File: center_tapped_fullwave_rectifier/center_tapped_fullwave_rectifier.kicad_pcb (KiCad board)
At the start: 2 copper layers, 47.5 x 21 mm, 5 parts, among them J1 Screw_Terminal_01x03, J2 Screw_Terminal_01x02

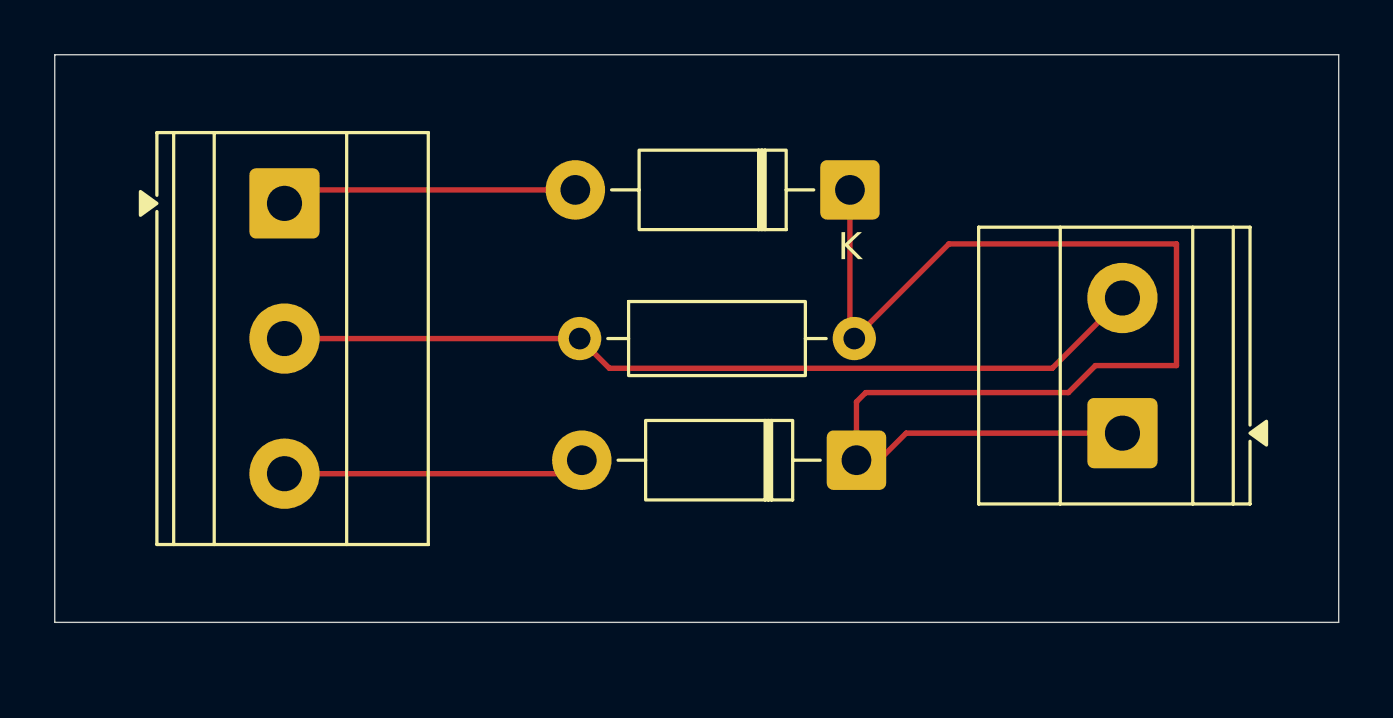
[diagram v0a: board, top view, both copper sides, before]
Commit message: Correct Footprint of transformer and reduced hole size
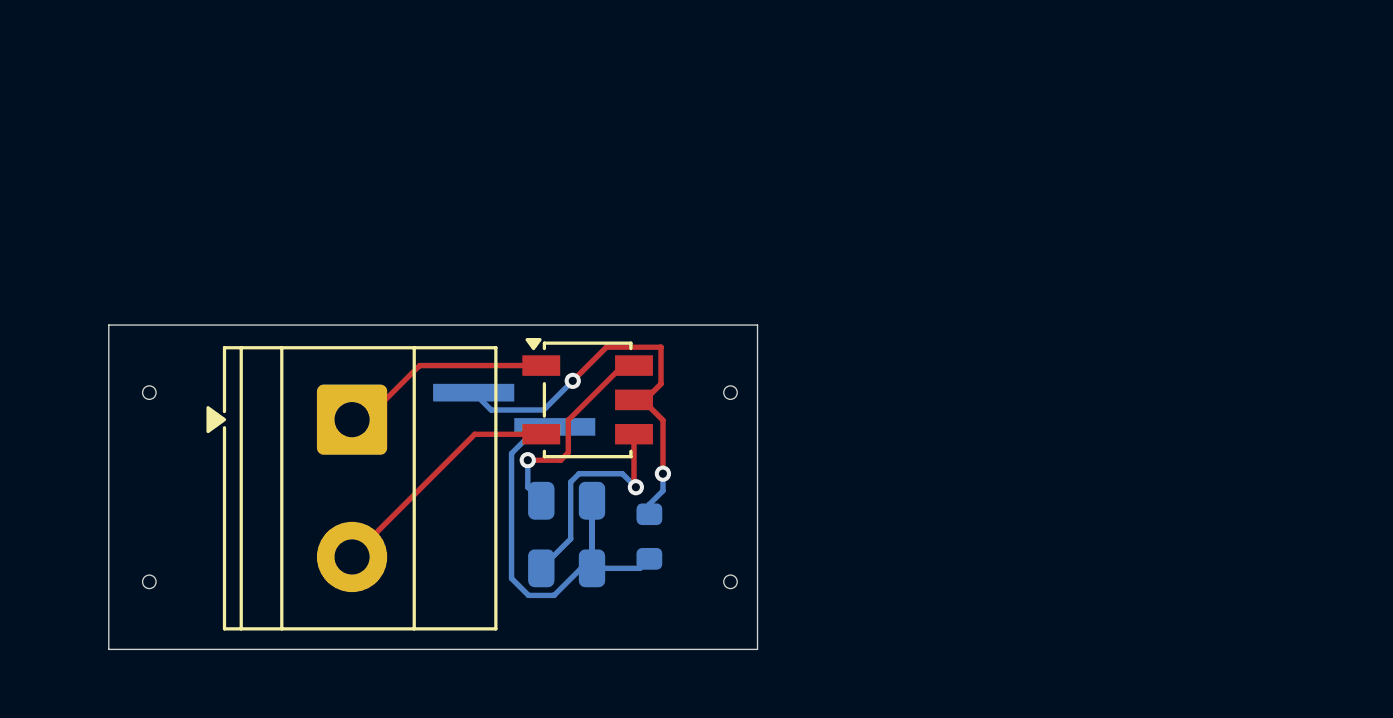
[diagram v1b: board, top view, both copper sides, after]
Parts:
- added H1: MountingHole, MountingHole:MountingHole_2.1mm, F.Cu at (125.5, 85.5)
- added H2: MountingHole, MountingHole:MountingHole_2.1mm, F.Cu at (125.5, 92.5)
- added H3: MountingHole, MountingHole:MountingHole_2.1mm, F.Cu at (104.0, 85.5)
- added H4: MountingHole, MountingHole:MountingHole_2.1mm, F.Cu at (104.0, 92.5)
- added T1: Transformer_1P_SS, Transformer_SMD:Transformer_MACOM_SM-22, F.Cu at (120.2, 85.8)
- D1, D2: footprint Diode_THT:D_DO-41_SOD81_P10.16mm_Horizontal -> Diode_SMD:D_0805_2012Metric; moved to B.Cu
- J1: value Screw_Terminal_01x03 -> Screw_Terminal_01x02; footprint TerminalBlock_Phoenix:TerminalBlock_Phoenix_MKDS-1,5-3_1x03_P5.00mm_Horizontal -> TerminalBlock_Phoenix:TerminalBlock_Phoenix_MKDS-1,5-2-5.08_1x02_P5.08mm_Horizontal
- J2: value Screw_Terminal_01x02 -> Conn_01x02_Pin; footprint TerminalBlock_Phoenix:TerminalBlock_Phoenix_MKDS-1,5-2_1x02_P5.00mm_Horizontal -> Connector_PinHeader_1.27mm:PinHeader_1x02_P1.27mm_Vertical_SMD_Pin1Right; moved to B.Cu
- R1: footprint Resistor_THT:R_Axial_DIN0207_L6.3mm_D2.5mm_P10.16mm_Horizontal -> Resistor_SMD:R_0603_1608Metric; moved to B.Cu
- moved J2 22.5 mm to (117.5, 86.1), turned to 180 degrees
- moved D1 15.6 mm to (119.4, 89.5)
- moved D2 11.4 mm to (119.4, 92.0)
- moved J1 8.38 mm to (111.5, 86.5)
- moved R1 7.77 mm to (122.5, 90.8), turned to -90 degrees
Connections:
- J1 pad 1: Net-(D1-A) -> Net-(J1-Pin_1)
- J1 pad 2: GND -> Net-(J1-Pin_2)
- J2 pad 1: Net-(D1-K) -> Net-(J2-Pin_1)
- J2 pad 2: GND -> Net-(D1-K)
- R1 pad 1: GND -> Net-(J2-Pin_1)
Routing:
- net GND: track 32.5 -> 0.00 mm
- net Net-(D1-K): track 48.4 -> 17.3 mm
- net Net-(J2-Pin_1): track 0.00 -> 15.8 mm, vias 0 -> 2
- net Net-(J1-Pin_2): track 0.00 -> 8.88 mm
- net Net-(J1-Pin_1): track 0.00 -> 7.83 mm
- net Net-(D1-A): track 11.0 -> 7.79 mm, vias 0 -> 1
- net Net-(D2-A): track 11.2 -> 8.38 mm, vias 0 -> 1
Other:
- board size 47.5 x 21 mm -> 24 x 12 mm

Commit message: Gerber files added
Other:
- board size 24 x 12 mm -> 27.5 x 13 mm
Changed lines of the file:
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@@
 		(filling no)
 		(pcbplotparams
-			(layerselection 0x00000000_00000000_55555555_5755f5ff)
+			(layerselection 0x00000000_00000000_55557fdf_57ffffff)
 			(plot_on_all_layers_selection 0x00000000_00000000_00000000_00000000)
 			(disableapertmacros no)
@@
 			(outputformat 1)
 			(mirror no)
-			(drillshape 1)
+			(drillshape 0)
 			(scaleselection 1)
 			(outputdirectory "")
@@
 	)
 	(gr_rect
-		(start 102.5 83)
-		(end 126.5 95)
+		(start 101 82.5)
+		(end 128.5 95.5)
 		(stroke
 			(width 0.05)
